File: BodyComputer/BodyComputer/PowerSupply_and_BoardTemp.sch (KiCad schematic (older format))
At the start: 48 parts

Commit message: Update due to moving to another computer. Updated Schematic, Print-outs, PCB in development
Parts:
- removed R? (x2): 10k, Resistor_SMD:R_0603_1608Metric, symbol Device:R
- removed TH? (x2): NTC_100k, Resistor_SMD:R_0402_1005Metric, symbol Device:Thermistor_NTC
- D10, D8, D9: renamed from D?; footprint (none) -> Diode_SMD:D_0603_1608Metric_Pad1.05x0.95mm_HandSolder
- D3, D7: renamed from D?; footprint (none) -> Diode_SMD:D_SOD-323_HandSoldering
- J3, J4, J5, J6: renamed from J?; footprint (none) -> SamacSys_Parts:SHDR3W95P0X500_1X3_1620X900X1280P
- U1, U2: renamed from U?; footprint (none) -> Package_TO_SOT_SMD:SOT-223
- gave numbers to parts that had none: 30
- renumbered R3 to R10, R2 to R11, R1 to R12

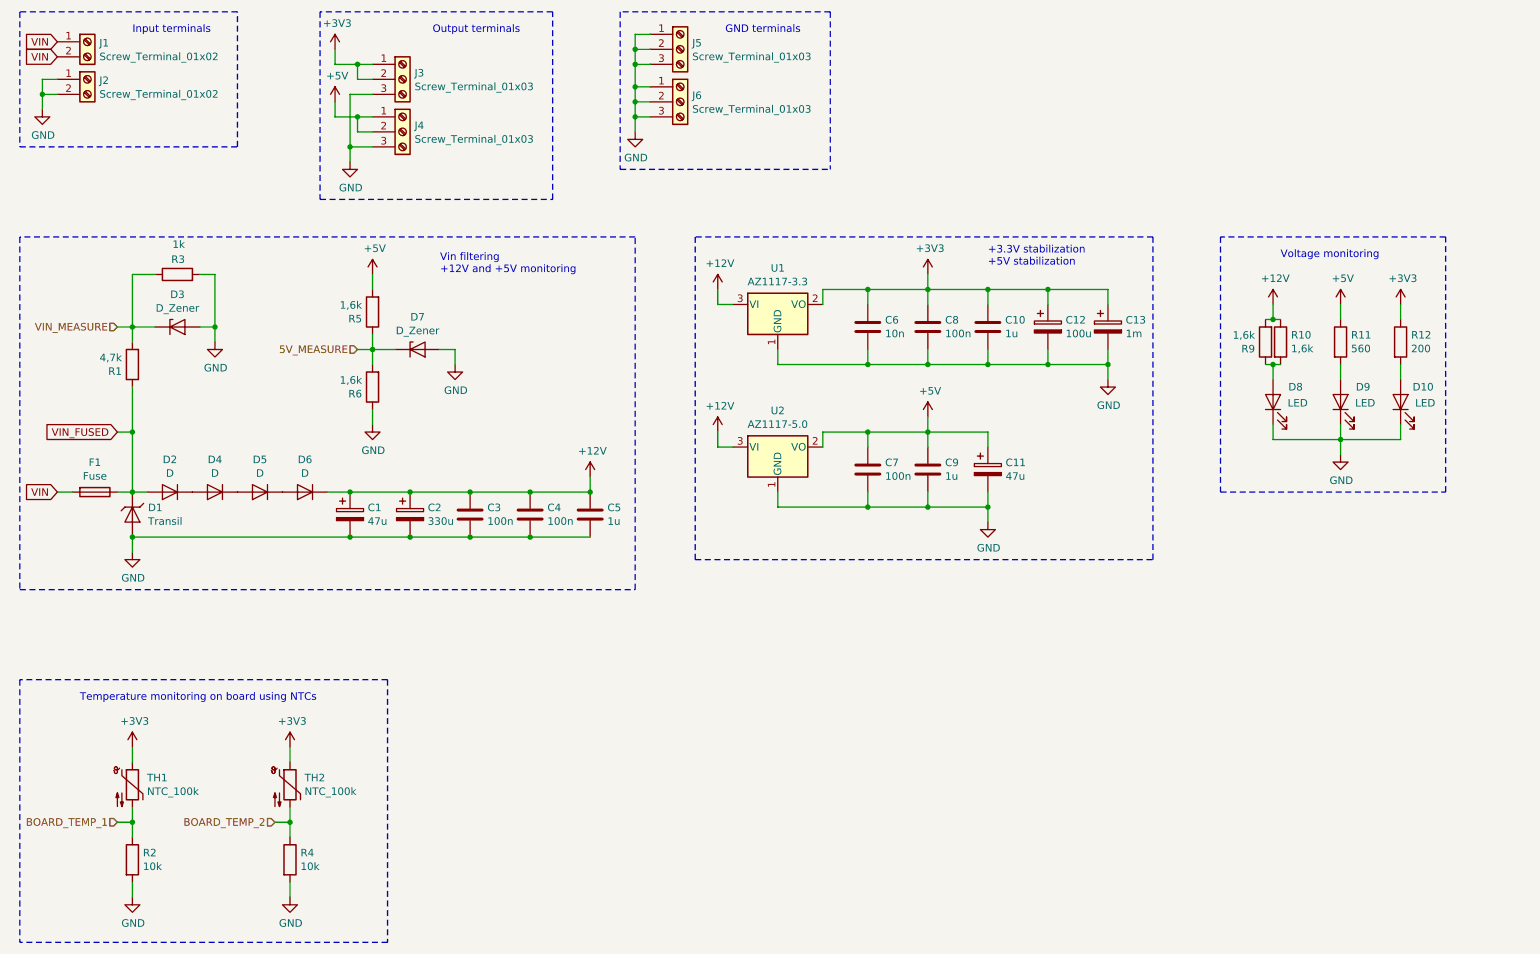
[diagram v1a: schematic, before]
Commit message: Updated schematic (DC/DC), 2-layer PCB
Updated schematic in multiple places, added elements, exchanged 3V3 stabilizer for a DC/DC converter. Nearly finished 2-layer PCB layout.
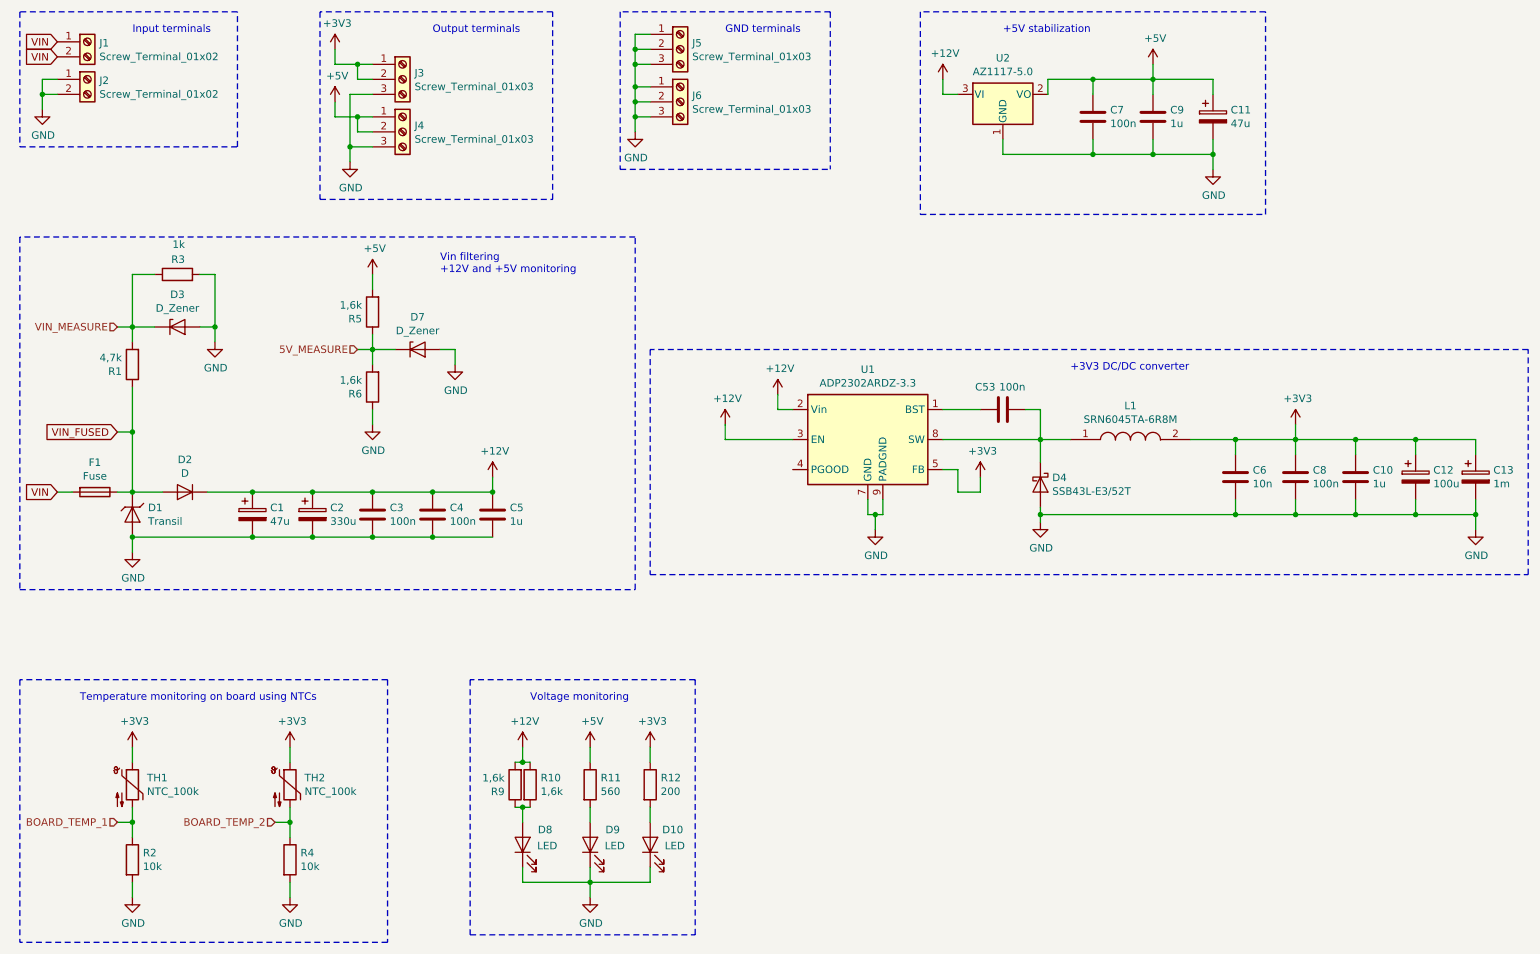
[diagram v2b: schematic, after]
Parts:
- removed D4, D5, D6: D, Diode_SMD:D_SMC_Handsoldering, symbol Device:D
- removed U1: AZ1117-3.3, Package_TO_SOT_SMD:SOT-223, symbol Regulator_Linear:AZ1117-3.3
- added C53: 100n, Capacitor_SMD:C_0603_1608Metric, symbol Device:C
- added D4: SSB43L-E3/52T, Diode_SMD:D_SMB, symbol Device:D_Schottky
- added L1: SRN6045TA-6R8M, SRN6045TA-6R8M, symbol SamacSys_Parts:SRN6045TA-6R8M
- added U1: ADP2302ARDZ-3.3, Package_SO:SOIC-8-1EP_3.9x4.9mm_P1.27mm_EP2.29x3mm, symbol Regulator_Switching:ADP2302ARDZ-3.3
- D1: footprint Diode_SMD:D_SMB_Handsoldering -> Diode_SMD:D_SMB
- D2: footprint Diode_SMD:D_SMC_Handsoldering -> Diode_SMD:D_SMC
- U2: footprint Package_TO_SOT_SMD:SOT-223 -> Package_TO_SOT_SMD:SOT-223-3_TabPin2
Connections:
- net +12V: now also D2.1 (K), U1.2 (Vin), U1.3 (EN)
- net +3V3: now also L1.2, U1.5 (FB)
- net GND: now also D4.2 (A), U1.7 (GND), U1.9 (PADGND)
- new net: C53.1, U1.1 (BST)
- new net: C53.2, D4.1 (K), L1.1, U1.8 (SW)
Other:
- note added: "+3V3 DC/DC converter"
- note added: "+5V stabilization"
- note removed: "+3.3V stabilization\n+5V stabilization"
- moved on the sheet: C1, C10, C11, C12, C13, C2, C3, C4, C5, C6, C7, C8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

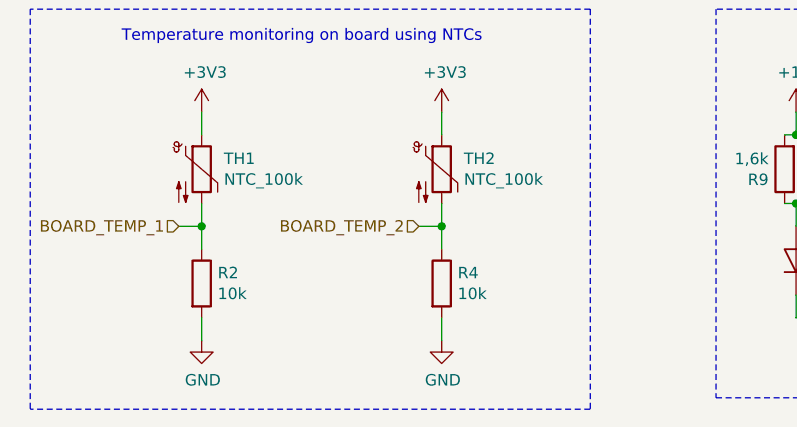
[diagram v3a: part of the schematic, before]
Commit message: Body Computer [DONE]
Body Computer done as a 2-layer board and put into prototype production, schematics and PCBs created.
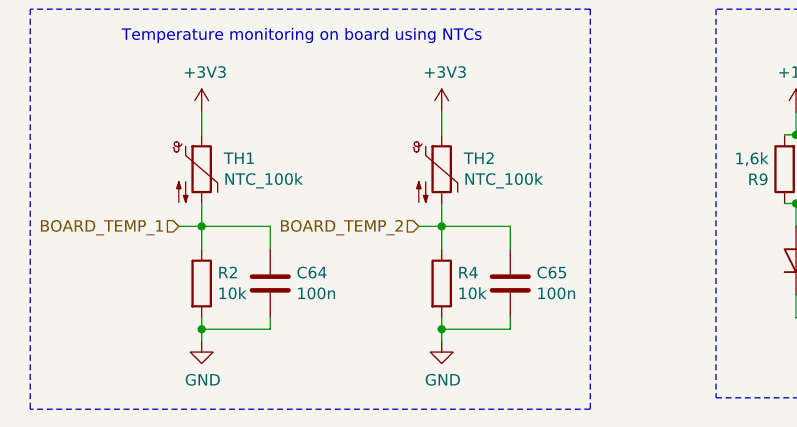
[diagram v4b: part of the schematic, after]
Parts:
- added C64, C65: 100n, Capacitor_SMD:C_0603_1608Metric, symbol Device:C
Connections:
- net BOARD_TEMP_1: now also C64.1
- net BOARD_TEMP_2: now also C65.1
- net GND: now also C64.2, C65.2
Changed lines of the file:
@@
 Sheet 2 7
 Title "Body Computer"
-Date "2020-04-12"
+Date "2020-04-17"
 Rev "1.0"
 Comp "Wojciech Grzeliński"
@@
 	1750 6000 1750 5900
 Wire Wire Line
-	1750 6800 1750 6900
+	1750 6800 1750 6850
 $Comp
 L power:GND #PWR?
@@
 $EndComp
 Wire Wire Line
-	2800 6800 2800 6900
+	2800 6800 2800 6850
 $Comp
 L power:GND #PWR?
@@
 Wire Wire Line
 	7400 4200 7400 4100
+$Comp
+L Device:C C?
+U 1 1 5F29B791
+P 2050 6650
+AR Path="/5E664F82/5F29B791" Ref="C?"  Part="1"
+AR Path="/5E667041/5F29B791" Ref="C64"  Part="1"
+F 0 "C64" H 2165 6696 50  0000 L CNN
+F 1 "100n" H 2165 6605 50  0000 L CNN
+F 2 "Capacitor_SMD:C_0603_1608Metric" H 2088 6500 50  0001 C CNN
+F 3 "~" H 2050 6650 50  0001 C CNN
+	1    2050 6650
+	1    0    0    -1
+$EndComp
+$Comp
+L Device:C C?
+U 1 1 5F2A2550
+P 3100 6650
+AR Path="/5E664F82/5F2A2550" Ref="C?"  Part="1"
+AR Path="/5E667041/5F2A2550" Ref="C65"  Part="1"
+F 0 "C65" H 3215 6696 50  0000 L CNN
+F 1 "100n" H 3215 6605 50  0000 L CNN
+F 2 "Capacitor_SMD:C_0603_1608Metric" H 3138 6500 50  0001 C CNN
+F 3 "~" H 3100 6650 50  0001 C CNN
+	1    3100 6650
+	1    0    0    -1
+$EndComp
+Wire Wire Line
+	2050 6800 2050 6850
+Wire Wire Line
+	2050 6850 1750 6850
+Connection ~ 1750 6850
+Wire Wire Line
+	1750 6850 1750 6900
+Wire Wire Line
+	2050 6500 2050 6400
+Wire Wire Line
+	2050 6400 1750 6400
+Wire Wire Line
+	3100 6500 3100 6400
+Wire Wire Line
+	3100 6400 2800 6400
+Wire Wire Line
+	3100 6800 3100 6850
+Wire Wire Line
+	3100 6850 2800 6850
+Connection ~ 2800 6850
+Wire Wire Line
+	2800 6850 2800 6900
 $EndSCHEMATC
